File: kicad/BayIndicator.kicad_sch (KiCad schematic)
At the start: 3 parts, among them J1_TOP Conn_02x04_Odd_Even, J2_BOTTOM Conn_02x04_Odd_Even, U1 XIAO ESP32C3

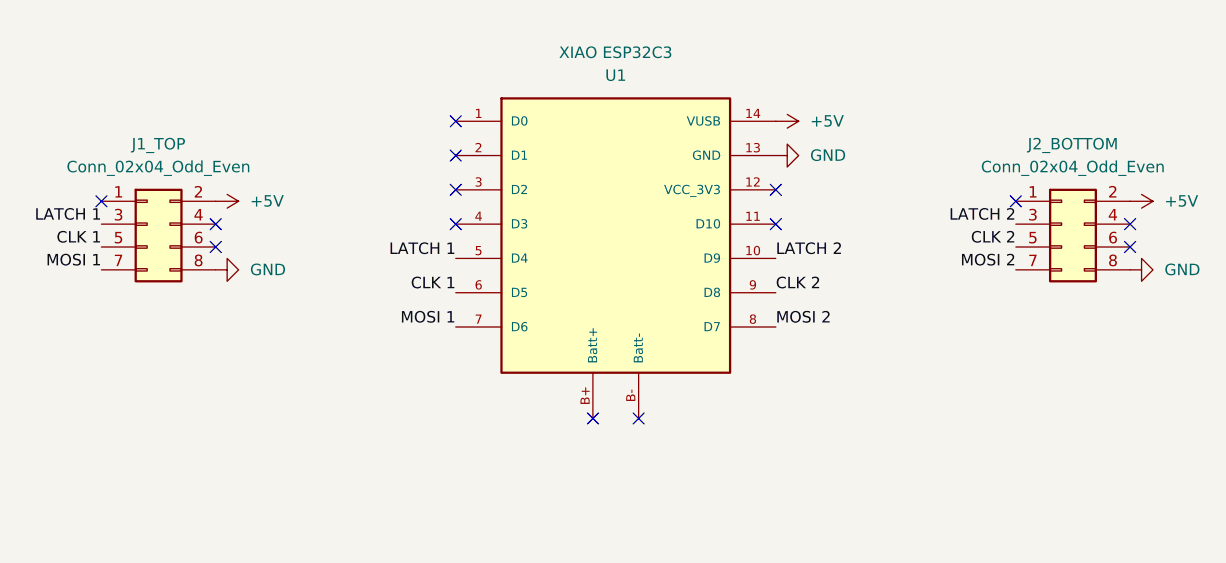
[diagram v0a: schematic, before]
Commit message: Adjust the schematic to match the current state
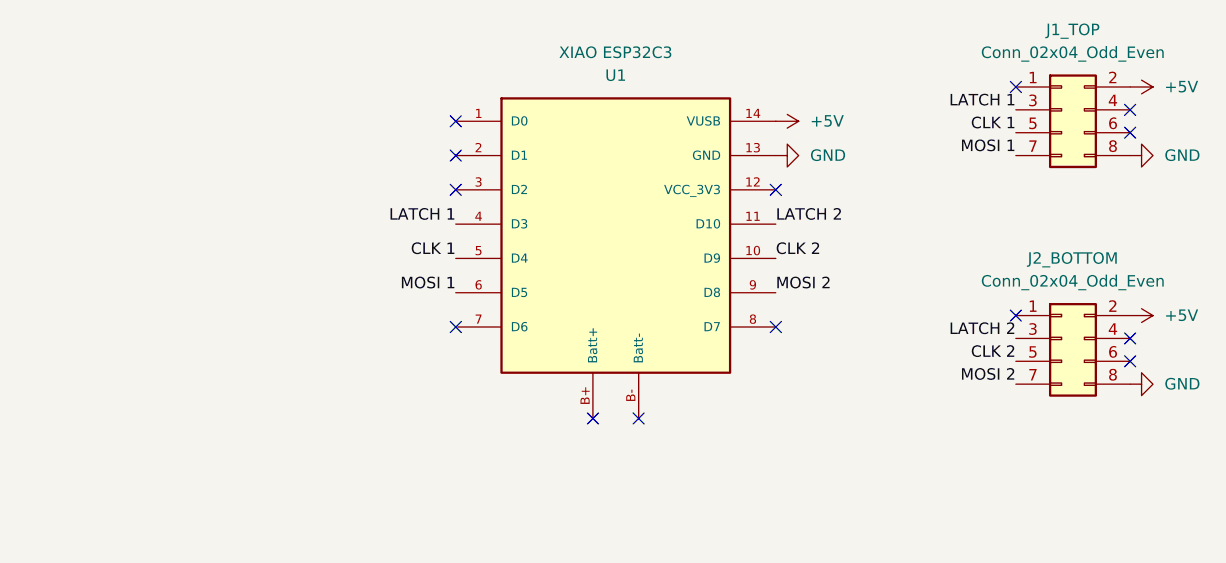
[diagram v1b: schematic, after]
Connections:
- net CLK 1: now also U1.5 (D4); no longer U1.6 (D5)
- net CLK 2: now also U1.10 (D9); no longer U1.9 (D8)
- net LATCH 1: now also U1.4 (D3); no longer U1.5 (D4)
- net LATCH 2: now also U1.11 (D10); no longer U1.10 (D9)
- net MOSI 1: now also U1.6 (D5); no longer U1.7 (D6)
- net MOSI 2: now also U1.9 (D8); no longer U1.8 (D7)
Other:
- moved on the sheet: J1_TOP, J2_BOTTOM

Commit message: Reconnect to match the actual state
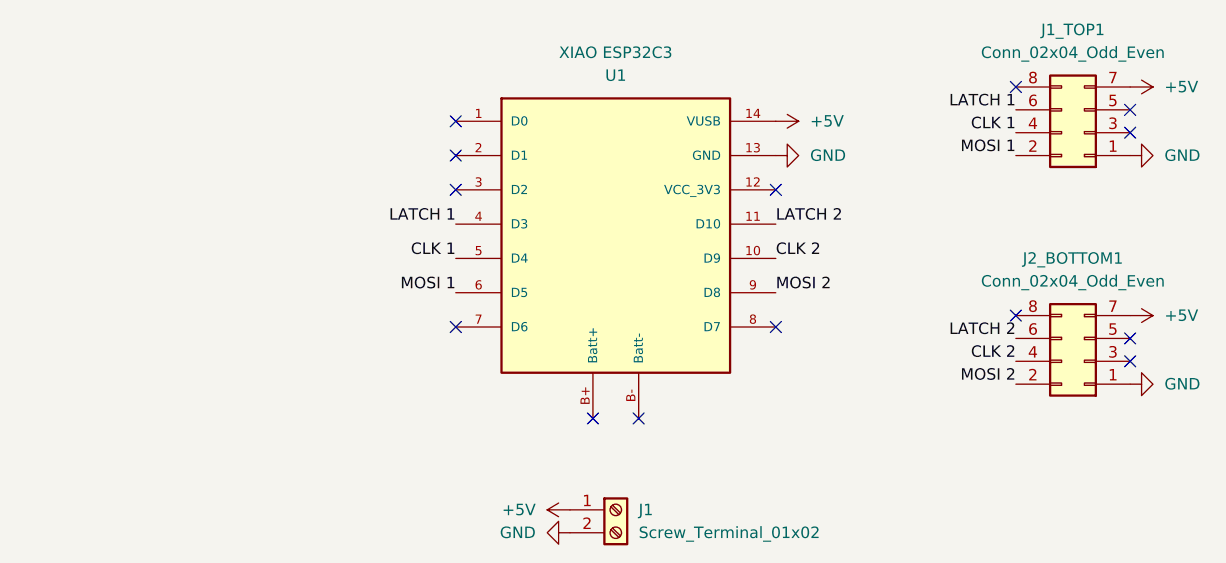
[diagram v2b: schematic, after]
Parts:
- added J1: Screw_Terminal_01x02, symbol Connector:Screw_Terminal_01x02
- J1_TOP1: renamed from J1_TOP; footprint (none) -> Connector_IDC:IDC-Header_2x04_P2.54mm_Vertical
- J2_BOTTOM1: renamed from J2_BOTTOM; footprint (none) -> Connector_IDC:IDC-Header_2x04_P2.54mm_Vertical
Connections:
- net +5V: now also J1_TOP1.7 (Pin_7), J2_BOTTOM1.7 (Pin_7), J1.1 (Pin_1); no longer J1_TOP1.2 (Pin_2), J2_BOTTOM1.2 (Pin_2)
- net CLK 1: now also J1_TOP1.4 (Pin_4); no longer J1_TOP1.5 (Pin_5)
- net CLK 2: now also J2_BOTTOM1.4 (Pin_4); no longer J2_BOTTOM1.5 (Pin_5)
- net GND: now also J1_TOP1.1 (Pin_1), J2_BOTTOM1.1 (Pin_1), J1.2 (Pin_2); no longer J1_TOP1.8 (Pin_8), J2_BOTTOM1.8 (Pin_8)
- net LATCH 1: now also J1_TOP1.6 (Pin_6); no longer J1_TOP1.3 (Pin_3)
- net LATCH 2: now also J2_BOTTOM1.6 (Pin_6); no longer J2_BOTTOM1.3 (Pin_3)
- net MOSI 1: now also J1_TOP1.2 (Pin_2); no longer J1_TOP1.7 (Pin_7)
- net MOSI 2: now also J2_BOTTOM1.2 (Pin_2); no longer J2_BOTTOM1.7 (Pin_7)
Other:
- moved on the sheet: J1_TOP1, J2_BOTTOM1
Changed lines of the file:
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@@
+	)
+	(symbol
+		(lib_id "Connector:Screw_Terminal_01x02")
+		(at 88.9 81.28 0)
+		(unit 1)
+		(exclude_from_sim no)
+		(in_bom yes)
+		(on_board yes)
+		(dnp no)
+		(fields_autoplaced yes)
+		(property "Reference" "J1"
+			(at 91.44 81.2799 0)
+			(effects
+				(font
+					(size 1.27 1.27)
+				)
+				(justify left)
+			)
+		)
+		(property "Value" "Screw_Terminal_01x02"
+			(at 91.44 83.8199 0)
+			(effects
+				(font
+					(size 1.27 1.27)
+				)
+				(justify left)
+			)
+		)
+		(property "Footprint" ""
+			(at 88.9 81.28 0)
+			(effects
+				(font
+					(size 1.27 1.27)
+				)
+				(hide yes)
+			)
+		)
+		(property "Datasheet" "~"
+			(at 88.9 81.28 0)
+			(effects
+				(font
+					(size 1.27 1.27)
+				)
+				(hide yes)
+			)
+		)
+		(property "Description" "Generic screw terminal, single row, 01x02, script generated (kicad-library-utils/schlib/autogen/connector/)"
+			(at 88.9 81.28 0)
+			(effects
+				(font
+					(size 1.27 1.27)
+				)
+				(hide yes)
+			)
+		)
+		(pin "2"
+		)
+		(pin "1"
+		)
+		(instances
+			(project ""
+				(path "/abca6d84-0381-4009-9124-d61ad9791431"
+					(reference "J1")
+					(unit 1)
+				)
+			)
+		)
+	)
+	(symbol
+		(lib_id "power:+5V")
+		(at 83.82 81.28 90)
+		(unit 1)
+		(exclude_from_sim no)
+		(in_bom yes)
+		(on_board yes)
+		(dnp no)
+		(fields_autoplaced yes)
+		(property "Reference" "#PWR07"
+			(at 87.63 81.28 0)
+			(effects
+				(font
+					(size 1.27 1.27)
+				)
+				(hide yes)
+			)
+		)
+		(property "Value" "+5V"
+			(at 80.01 81.2799 90)
+			(effects
+				(font
+					(size 1.27 1.27)
+				)
+				(justify left)
+			)
+		)
+		(property "Footprint" ""
+			(at 83.82 81.28 0)
+			(effects
+				(font
+					(size 1.27 1.27)
+				)
+				(hide yes)
+			)
+		)
+		(property "Datasheet" ""
+			(at 83.82 81.28 0)
+			(effects
+				(font
+					(size 1.27 1.27)
+				)
+				(hide yes)
+			)
+		)
+		(property "Description" "Power symbol creates a global label with name \"+5V\""
+			(at 83.82 81.28 0)
+			(effects
+				(font
+					(size 1.27 1.27)
+				)
+				(hide yes)
+			)
+		)
+		(pin "1"
+		)
+		(instances
+			(project "BayIndicator"
+				(path "/abca6d84-0381-4009-9124-d61ad9791431"
+					(reference "#PWR07")
+					(unit 1)
+				)
+			)
+		)
+	)
+	(symbol
+		(lib_id "power:GND")
+		(at 83.82 83.82 270)
+		(unit 1)
+		(exclude_from_sim no)
+		(in_bom yes)
+		(on_board yes)
+		(dnp no)
+		(fields_autoplaced yes)
+		(property "Reference" "#PWR08"
+			(at 77.47 83.82 0)
+			(effects
+				(font
+					(size 1.27 1.27)
+				)
+				(hide yes)
+			)
+		)
+		(property "Value" "GND"
+			(at 80.01 83.8199 90)
+			(effects
+				(font
+					(size 1.27 1.27)
+				)
+				(justify right)
+			)
+		)
+		(property "Footprint" ""
+			(at 83.82 83.82 0)
+			(effects
+				(font
+					(size 1.27 1.27)
+				)
+				(hide yes)
+			)
+		)
+		(property "Datasheet" ""
+			(at 83.82 83.82 0)
+			(effects
+				(font
+					(size 1.27 1.27)
+				)
+				(hide yes)
+			)
+		)
+		(property "Description" "Power symbol creates a global label with name \"GND\" , ground"
+			(at 83.82 83.82 0)
+			(effects
+				(font
+					(size 1.27 1.27)
+				)
+				(hide yes)
+			)
+		)
+		(pin "1"
+		)
+		(instances
+			(project "BayIndicator"
+				(path "/abca6d84-0381-4009-9124-d61ad9791431"
+					(reference "#PWR08")
+					(unit 1)
+				)
+			)
+		)
 	)
 	(symbol
@@
 	(symbol
 		(lib_id "Connector_Generic:Conn_02x04_Odd_Even")
-		(at 138.43 36.83 0)
-		(unit 1)
-		(exclude_from_sim no)
-		(in_bom yes)
-		(on_board yes)
-		(dnp no)
-		(fields_autoplaced yes)
-		(property "Reference" "J1_TOP"
+		(at 140.97 39.37 180)
+		(unit 1)
+		(exclude_from_sim no)
+		(in_bom yes)
+		(on_board yes)
+		(dnp no)
+		(fields_autoplaced yes)
+		(property "Reference" "J1_TOP1"
 			(at 139.7 27.94 0)
 			(effects
@@
 			)
 		)
-		(property "Footprint" ""
-			(at 138.43 36.83 0)
+		(property "Footprint" "Connector_IDC:IDC-Header_2x04_P2.54mm_Vertical"
+			(at 140.97 39.37 0)
 			(effects
 				(font
@@
 		)
 		(property "Datasheet" "~"
-			(at 138.43 36.83 0)
+			(at 140.97 39.37 0)
 			(effects
 				(font
@@
 		)
 		(property "Description" "Generic connector, double row, 02x04, odd/even pin numbering scheme (row 1 odd numbers, row 2 even numbers), script generated (kicad-library-utils/schlib/autogen/connector/)"
-			(at 138.43 36.83 0)
+			(at 140.97 39.37 0)
 			(effects
 				(font
@@
 			(project "BayIndicator"
 				(path "/abca6d84-0381-4009-9124-d61ad9791431"
-					(reference "J1_TOP")
+					(reference "J1_TOP1")
 					(unit 1)
 				)
@@
 	(symbol
 		(lib_id "Connector_Generic:Conn_02x04_Odd_Even")
-		(at 138.43 62.23 0)
-		(unit 1)
-		(exclude_from_sim no)
-		(in_bom yes)
-		(on_board yes)
-		(dnp no)
-		(fields_autoplaced yes)
-		(property "Reference" "J2_BOTTOM"
+		(at 140.97 64.77 180)
+		(unit 1)
+		(exclude_from_sim no)
+		(in_bom yes)
+		(on_board yes)
+		(dnp no)
+		(fields_autoplaced yes)
+		(property "Reference" "J2_BOTTOM1"
 			(at 139.7 53.34 0)
 			(effects
@@
 			)
 		)
-		(property "Footprint" ""
-			(at 138.43 62.23 0)
+		(property "Footprint" "Connector_IDC:IDC-Header_2x04_P2.54mm_Vertical"
+			(at 140.97 64.77 0)
 			(effects
 				(font
@@
 		)
 		(property "Datasheet" "~"
-			(at 138.43 62.23 0)
+			(at 140.97 64.77 0)
 			(effects
 				(font
@@
 		)
 		(property "Description" "Generic connector, double row, 02x04, odd/even pin numbering scheme (row 1 odd numbers, row 2 even numbers), script generated (kicad-library-utils/schlib/autogen/connector/)"
-			(at 138.43 62.23 0)
+			(at 140.97 64.77 0)
 			(effects
 				(font
@@
 			(project "BayIndicator"
 				(path "/abca6d84-0381-4009-9124-d61ad9791431"
-					(reference "J2_BOTTOM")
-					(unit 1)
-				)
+					(reference "J2_BOTTOM1")
+					(unit 1)
+				)

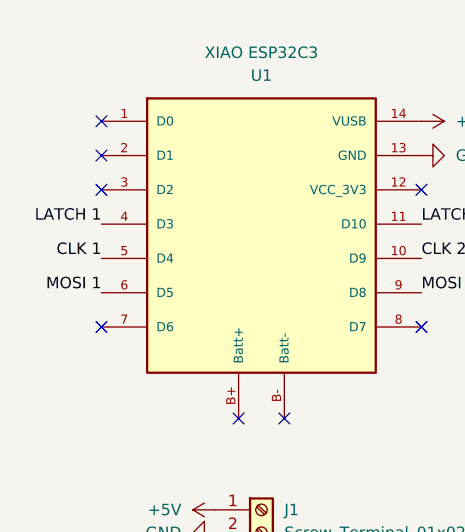
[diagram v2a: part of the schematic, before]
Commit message: Create a PCB for the BayIndicator
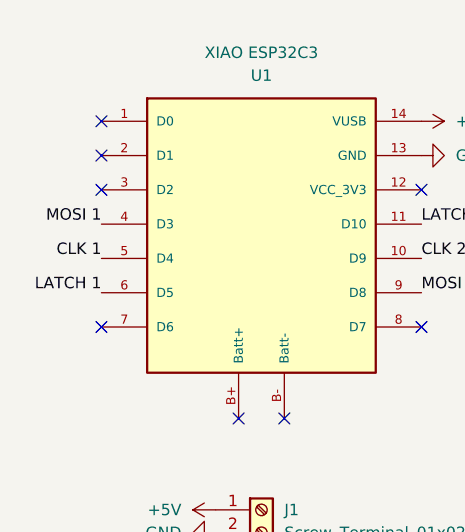
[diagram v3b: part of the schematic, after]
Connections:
- net LATCH 1: now also U1.6 (D5); no longer U1.4 (D3)
- net MOSI 1: now also U1.4 (D3); no longer U1.6 (D5)
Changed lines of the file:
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@@
 		)
 	)
-	(label "CLK 2"
-		(at 133.35 64.77 180)
+	(label "MOSI 1"
+		(at 71.12 49.53 180)
 		(effects
 			(font
@@
 		)
 	)
-	(label "MOSI 1"
-		(at 71.12 57.15 180)
+	(label "CLK 2"
+		(at 133.35 64.77 180)
 		(effects
 			(font
@@
 	)
 	(label "LATCH 1"
-		(at 71.12 49.53 180)
+		(at 71.12 57.15 180)
 		(effects
 			(font

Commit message: PCB design
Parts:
- J1: footprint (none) -> TerminalBlock:TerminalBlock_MaiXu_MX126-5.0-02P_1x02_P5.00mm
- renumbered J2_BOTTOM1 to JBOTTOM1, J1_TOP1 to JTOP1
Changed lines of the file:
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@@
 			)
 		)
-		(property "Footprint" ""
+		(property "Footprint" "TerminalBlock:TerminalBlock_MaiXu_MX126-5.0-02P_1x02_P5.00mm"
 			(at 88.9 81.28 0)
 			(hide yes)
@@
 		(dnp no)
 		(fields_autoplaced yes)
-		(property "Reference" "J1_TOP1"
+		(property "Reference" "JTOP1"
 			(at 139.7 27.94 0)
 			(show_name no)
@@
 			(project "BayIndicator"
 				(path "/abca6d84-0381-4009-9124-d61ad9791431"
-					(reference "J1_TOP1")
+					(reference "JTOP1")
 					(unit 1)
 				)
@@
 		(dnp no)
 		(fields_autoplaced yes)
-		(property "Reference" "J2_BOTTOM1"
+		(property "Reference" "JBOTTOM1"
 			(at 139.7 53.34 0)
 			(show_name no)
@@
 			(project "BayIndicator"
 				(path "/abca6d84-0381-4009-9124-d61ad9791431"
-					(reference "J2_BOTTOM1")
-					(unit 1)
-				)
+					(reference "JBOTTOM1")
+					(unit 1)
+				)
